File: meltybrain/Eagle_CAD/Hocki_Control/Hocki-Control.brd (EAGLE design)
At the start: 87 x 44 mm, 92 parts, among them U1 TEENSY_4.1, U10 TLV3502AIDCNR, U11 NL27WZ32USG, U12 NL27WZ32USG, U13 HMC1052L-TR, U14 LMV358, U15 IRF7509, U16 TMUX1219DCKR, U17 LMV358, U18 LMV358, U2 ADXL375, U3 ADXL375, U4 ADXL375, U5 ADXL375, U6 LMH6612MAX/NOPB, U7 LMH6612MAX/NOPB, U8 LMH6612MAX/NOPB, U9 LMH6612MAX/NOPB

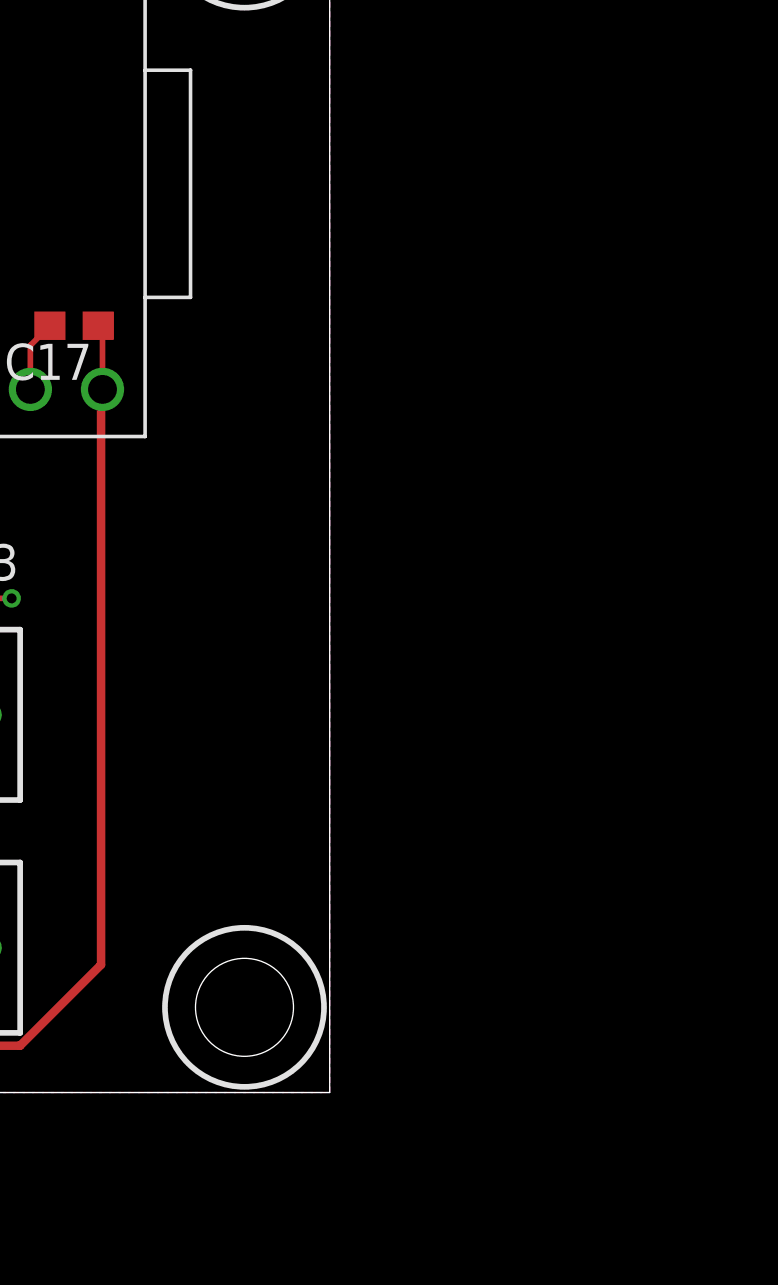
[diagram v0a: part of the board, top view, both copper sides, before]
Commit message: Added jst-sr connector and edited text labels
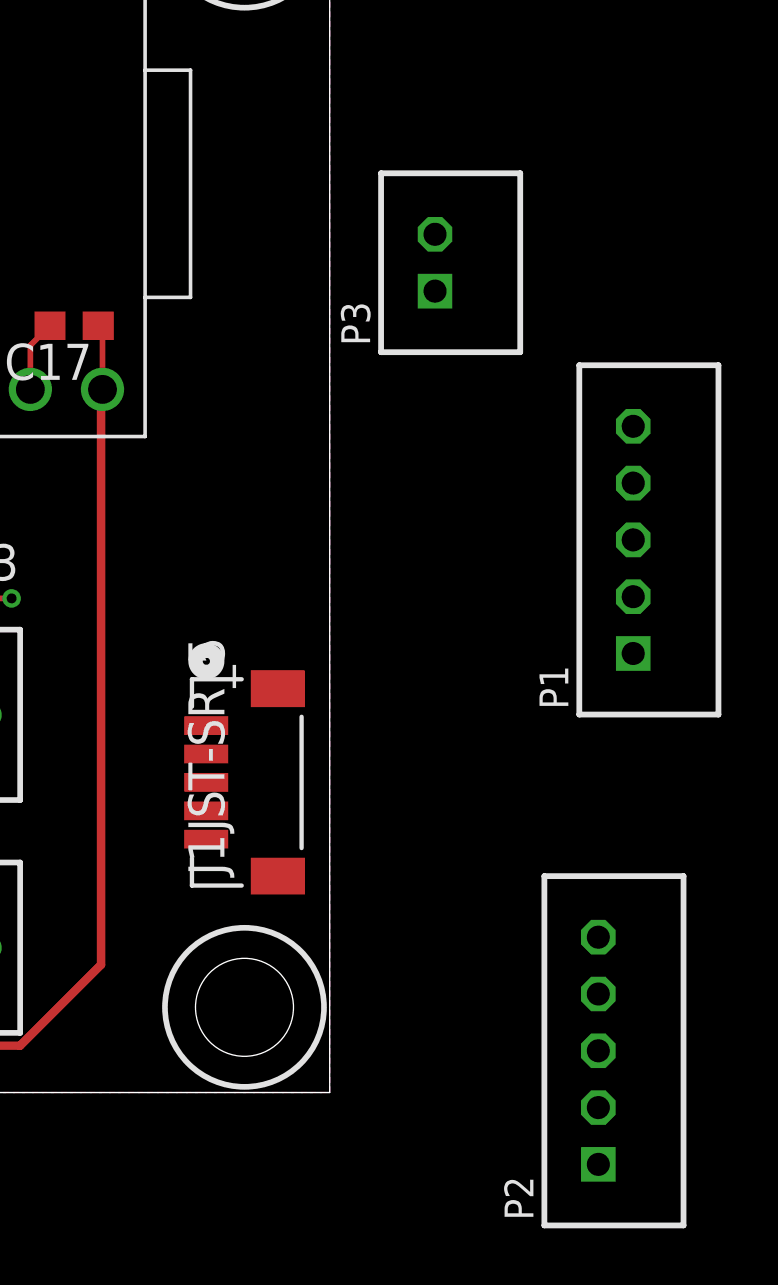
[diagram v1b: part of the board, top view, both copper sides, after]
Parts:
- added J1: JST-SR_5, Hocki_Library:CONN_BM05B-SRSS-TB_JST
- added P1, P2: B5B-PH-K, con-jst-ph:B5B-PH-K
- added P3: B2B-PH-K, con-jst-ph:B2B-PH-K
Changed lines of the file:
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@@
 <?xml version="1.0" encoding="utf-8"?>
 <!DOCTYPE eagle SYSTEM "eagle.dtd">
-<eagle version="9.5.2">
+<eagle version="9.6.2">
 <drawing>
 <settings>
-<setting alwaysvectorfont="yes"/>
+<setting alwaysvectorfont="no"/>
 <setting verticaltext="up"/>
 </settings>
-<grid distance="1" unitdist="mm" unit="mm" style="lines" multiple="1" display="no" altdistance="0.1" altunitdist="mm" altunit="mm"/>
+<grid distance="0.01" unitdist="mm" unit="mm" style="lines" multiple="1" display="no" altdistance="0.1" altunitdist="mm" altunit="mm"/>
 <layers>
 <layer number="1" name="Top" color="4" fill="1" visible="yes" active="yes"/>
@@
 <layer number="43" name="vRestrict" color="2" fill="10" visible="no" active="yes"/>
 <layer number="44" name="Drills" color="7" fill="1" visible="no" active="yes"/>
-<layer number="45" name="Holes" color="7" fill="1" visible="yes" active="yes"/>
+<layer number="45" name="Holes" color="7" fill="1" visible="no" active="yes"/>
 <layer number="46" name="Milling" color="3" fill="1" visible="no" active="yes"/>
 <layer number="47" name="Measures" color="7" fill="1" visible="no" active="yes"/>
@@
 <attribute name="VALUE" x="-43.3" y="-21.1" size="1" layer="27" align="top-left"/>
 </element>
+<element name="P1" library="con-jst-ph" package="B5B-PH-K" value="B5B-PH-K" x="48.69" y="-5.54" smashed="yes" rot="R90">
+<attribute name="LABEL" value="" x="48.69" y="-5.54" size="1.778" layer="27" rot="R90" display="off"/>
+<attribute name="NAME" x="46.404" y="-11.509" size="1.016" layer="25" ratio="18" rot="R90"/>
+<attribute name="VALUE" x="50.595" y="-10.62" size="1.016" layer="27" ratio="10" rot="R90"/>
+</element>
+<element name="P2" library="con-jst-ph" package="B5B-PH-K" value="B5B-PH-K" x="47.46" y="-23.53" smashed="yes" rot="R90">
+<attribute name="LABEL" value="" x="47.46" y="-23.53" size="1.778" layer="27" rot="R90" display="off"/>
+<attribute name="NAME" x="45.174" y="-29.499" size="1.016" layer="25" ratio="18" rot="R90"/>
+<attribute name="VALUE" x="49.365" y="-28.61" size="1.016" layer="27" ratio="10" rot="R90"/>
+</element>
+<element name="P3" library="con-jst-ph" package="B2B-PH-K" value="B2B-PH-K" x="41.71" y="4.22" smashed="yes" rot="R90">
+<attribute name="LABEL" value="" x="41.71" y="4.22" size="1.778" layer="27" rot="R90" display="off"/>
+<attribute name="NAME" x="39.424" y="1.299" size="1.016" layer="25" ratio="18" rot="R90"/>
+<attribute name="VALUE" x="43.615" y="2.315" size="1.016" layer="27" ratio="10" rot="R90"/>
+</element>
+<element name="J1" library="Hocki_Library" package="CONN_BM05B-SRSS-TB_JST" value="JST-SR_5" x="35.08" y="-14.08" smashed="yes" rot="R90">
+<attribute name="BUILT_BY" value="EMA_Cory" x="35.08" y="-14.08" size="1.778" layer="27" rot="R90" display="off"/>
+<attribute name="COPYRIGHT" value="Copyright (C) 2018 Accelerated Designs. All rights reserved" x="35.08" y="-14.08" size="1.778" layer="27" rot="R90" display="off"/>
+<attribute name="DATASHEET" value="http://www.jst-mfg.com/product/pdf/eng/eSR.pdf" x="35.08" y="-14.08" size="1.778" layer="27" rot="R90" display="off"/>
+<attribute name="DKPN" value="455-1791-1-ND" x="35.08" y="-14.08" size="1.778" layer="27" rot="R90" display="off"/>
+<attribute name="NAME" x="34.2926" y="-17.3566" size="1.27" layer="25" ratio="6" rot="SR90"/>
+<attribute name="SOURCELIBRARY" value="JST_2020-07-08" x="35.08" y="-14.08" size="1.778" layer="27" rot="R90" display="off"/>
+<attribute name="VALUE" x="34.2926" y="-15.8072" size="1.27" layer="21" ratio="6" rot="SR90"/>
+<attribute name="VENDOR" value="JST" x="35.08" y="-14.08" size="1.778" layer="27" rot="R90" display="off"/>
+</element>
 </elements>

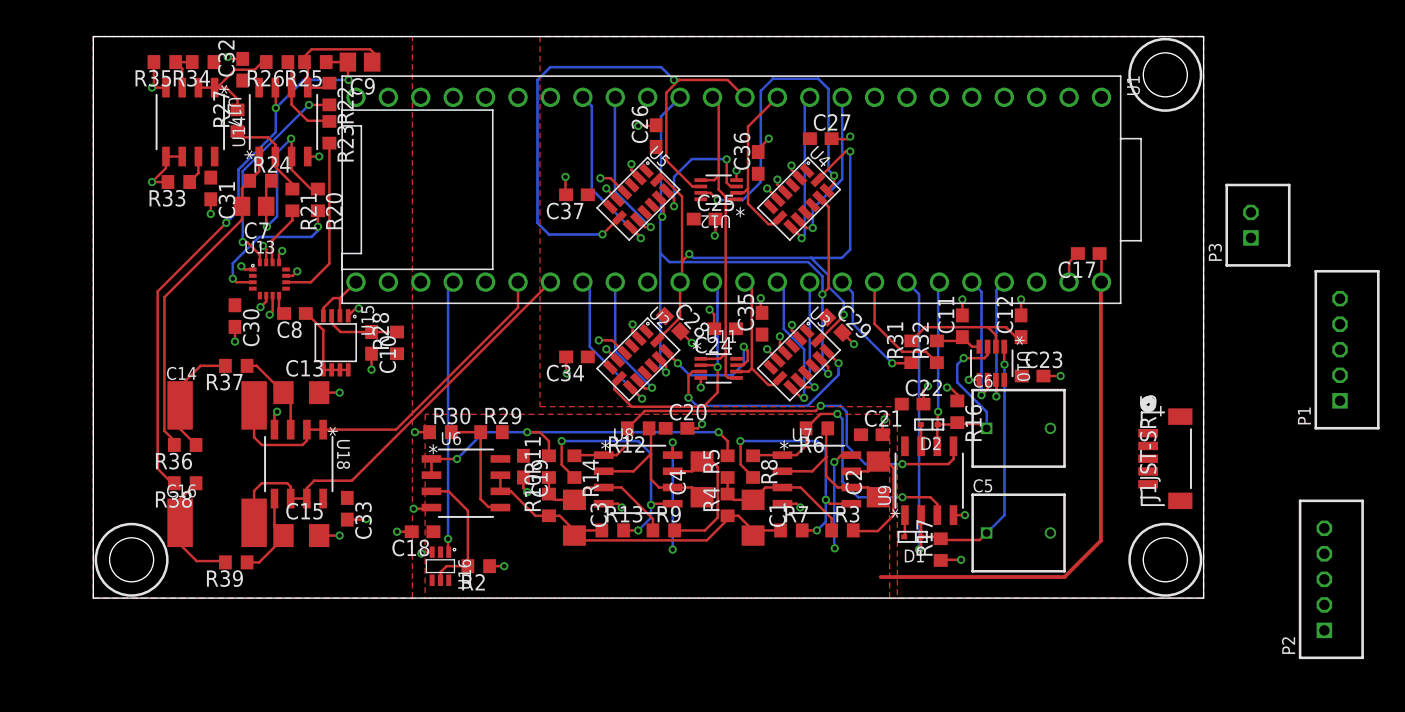
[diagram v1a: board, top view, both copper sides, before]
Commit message: started control power
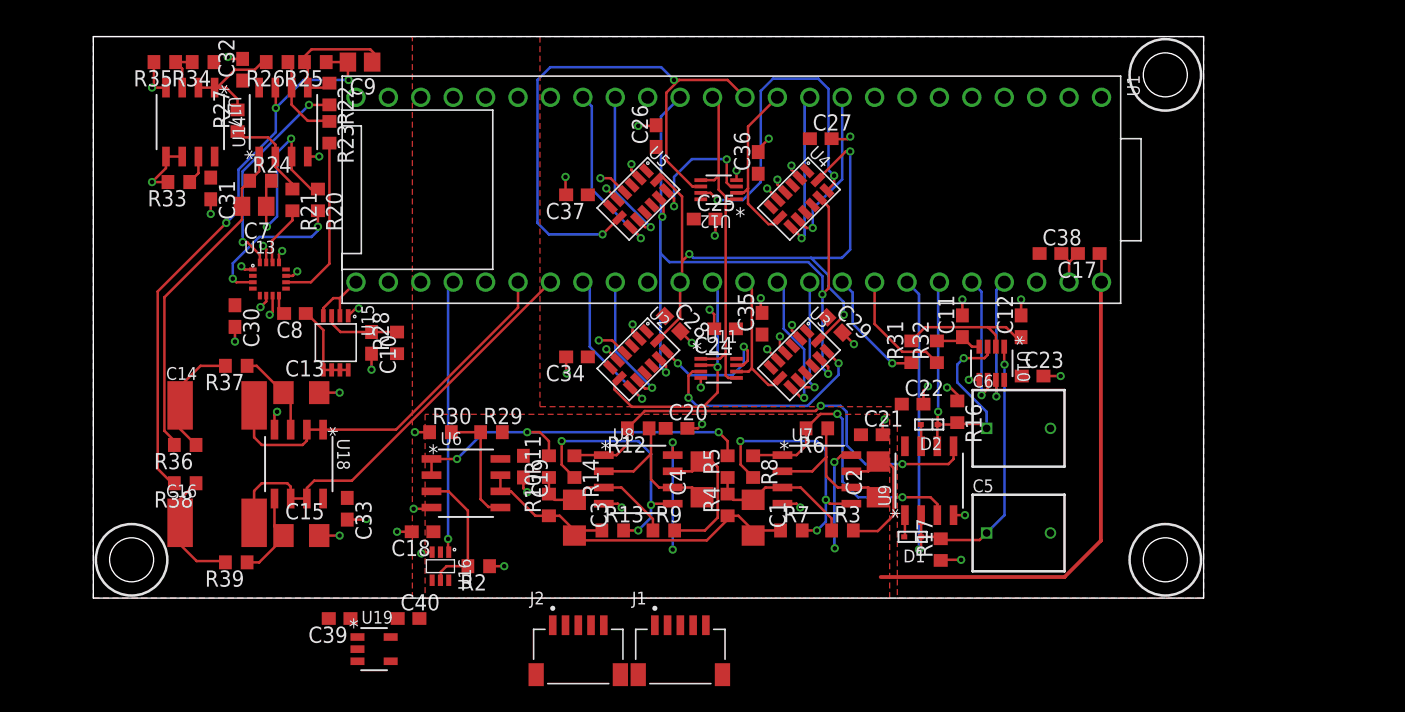
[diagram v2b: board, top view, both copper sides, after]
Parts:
- removed P1, P2: B5B-PH-K, con-jst-ph:B5B-PH-K
- removed P3: B2B-PH-K, con-jst-ph:B2B-PH-K
- added C38: 0.1u, rcl:C0603
- added C39, C40: 1u, rcl:C0603
- added J2: SM05B-SRSS-TB(LF)(SN), Hocki_Library:SM05B-SRSS-TB(LF)(SN)
- added U19: TLV73310PDBVT, Hocki_Library:SOT-23-5
- J1: value JST-SR_5 -> SM05B-SRSS-TB(LF)(SN); device Hocki_Library:CONN_BM05B-SRSS-TB_JST -> Hocki_Library:SM05B-SRSS-TB(LF)(SN)
- moved J1 41.7 mm to (-3.00, -31.0), turned to 0 degrees
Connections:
- new net +3V3: C30.1, C32.1, C33.1, C40.1, R28.1, R34.1, U13.4, U14.8, U18.8, U19.5
- new net N$5: C31.1, U17.8
- net 3.3V: now also C38.1, U1.3.3V1, U1.3.3V2; no longer C30.1, C31.1, C32.1, C33.1, R28.1, R34.1, U13.4, U14.8, U17.8, U18.8
- net 5V: now also C39.1, U19.1, U19.3
- net GND: now also C38.2, C39.2, C40.2, U19.2
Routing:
- net GND: track 86.9 -> 89.2 mm

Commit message: added IR connectors
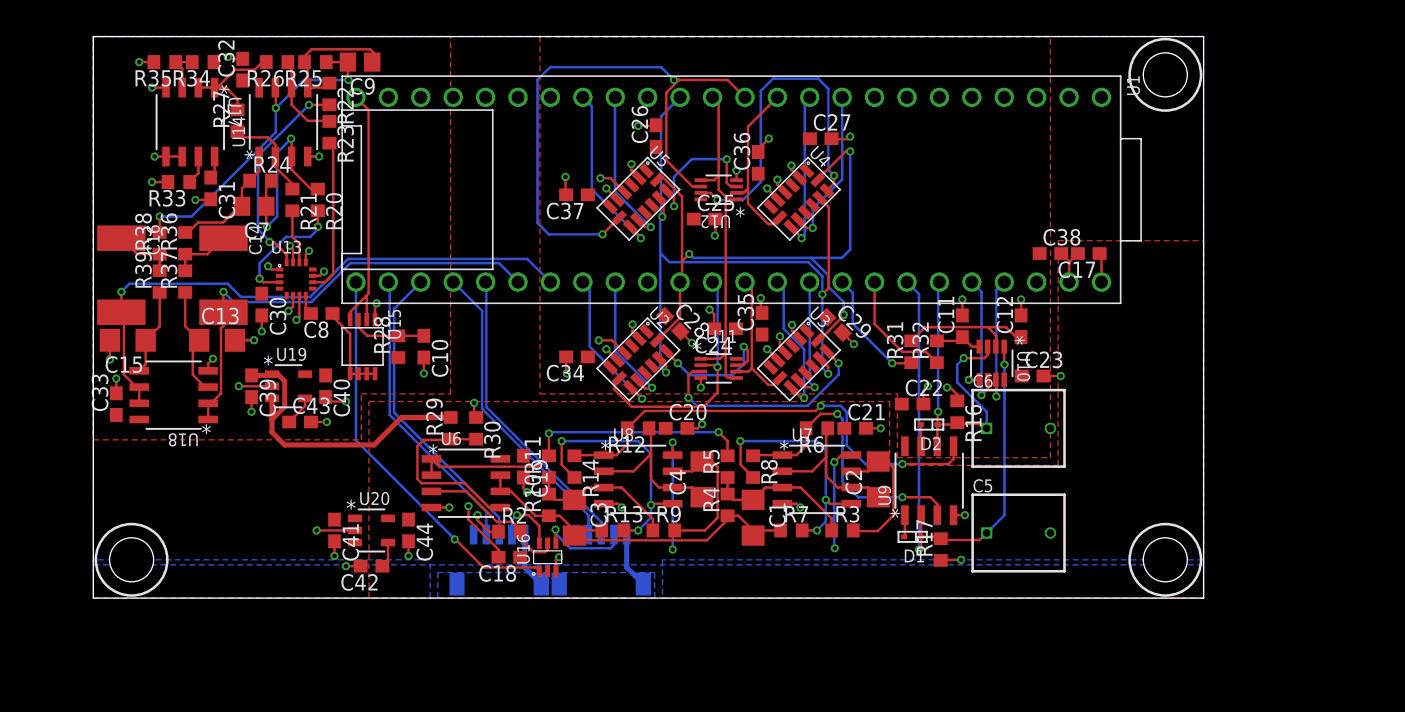
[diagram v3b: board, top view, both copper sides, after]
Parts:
- added C41: 1u, rcl:C0603
- added C42, C43: 100p, rcl:C0603
- added C44: 2.2u, rcl:C0603
- added U20: AP2210K-5.0TRG1, Hocki_Library:SOT-23-5
- C40: value 1u -> 2.2u
- U19: value TLV73310PDBVT -> AP2210K-3.3TRG1
- moved R39 22.8 mm to (-43.8, -0.20), turned to 90 degrees
- moved U19 21.7 mm to (-33.7, -8.40)
- moved C16 20.8 mm to (-46.8, 0.30), turned to 270 degrees
- moved C15 20.5 mm to (-46.3, -4.80), turned to 180 degrees
- moved C33 19.9 mm to (-47.2, -9.80), turned to 90 degrees
- moved C39 19.5 mm to (-36.6, -8.40), turned to 270 degrees
- moved C40 19.3 mm to (-30.8, -8.40), turned to 270 degrees
- moved R38 18.9 mm to (-43.8, 2.80), turned to 90 degrees
- moved R36 15.8 mm to (-41.8, 2.80), turned to 90 degrees
- moved U18 11.2 mm to (-42.7, -9.10), turned to 180 degrees
- moved C14 10.2 mm to (-38.8, 0.30), turned to 270 degrees
- moved J1 9.43 mm to (-9.20, -23.9), flipped to the bottom
- moved J2 9.43 mm to (-17.2, -23.9), flipped to the bottom
- moved U16 8.43 mm to (-13.4, -21.8), turned to 90 degrees
- moved C13 7.77 mm to (-39.3, -4.80)
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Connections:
- removed net N$5: C31.1, U17.8
- new net 9V: C41.1, J1.1, J1.S1, J1.S2, J2.1, J2.S1, J2.S2, U20.1, U20.3
- new net IR_BOTTOM_A0: J2.3, U1.35
- new net IR_BOTTOM_A1: J2.4, U1.34
- new net IR_TOP_A0: J1.3, U1.37
- new net IR_TOP_A1: J1.4, U1.36
- new net N$11: C43.1, U19.4
- new net N$8: C42.1, U20.4
- net +3V3: now also C31.1, U17.8
- net 5V: now also C44.1, U20.5
- net GND: now also C41.2, C42.2, C43.2, C44.2, J1.5, J2.5, U20.2
- net IR_BOTTOM: now also J2.2
- net IR_SEL: now also U1.33; no longer U1.36
- net IR_TOP: now also J1.2
- net S/R: now also U1.32; no longer U1.33
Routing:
- net IR_TOP_A1: track 0.00 -> 24.2 mm
- net IR_BOTTOM_A0: track 0.00 -> 24.1 mm
- net IR_TOP_A0: track 0.00 -> 23.6 mm
- net IR_BOTTOM_A1: track 0.00 -> 23.0 mm
- net MAG_OUTPUTB: track 45.2 -> 26.3 mm
- net MAG_OUTPUTA: track 26.0 -> 9.76 mm
- net GND: track 89.2 -> 105.4 mm, vias 60 -> 70
- net S/R: track 5.39 -> 20.3 mm
- net 5V: track 58.8 -> 44.3 mm
- net MAG_FILT_B: track 34.5 -> 45.8 mm, vias 0 -> 1
- net IR_SEL: track 21.3 -> 31.0 mm
- net 9V: track 0.00 -> 8.87 mm
- net IR_TOP: track 0.00 -> 7.36 mm, vias 0 -> 1
- net N$25: track 10.6 -> 4.82 mm
- net MAG_FILT_A: track 30.4 -> 35.9 mm, vias 0 -> 1
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- added copper zone on layer 1, net +3V3
- added copper zone on layer 16, net 9V
